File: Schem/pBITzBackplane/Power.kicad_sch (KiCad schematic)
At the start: 16 parts, among them J1 ATX-24, Q1 BSS138, SW1 SW_Push, U1 ATtiny85-20P

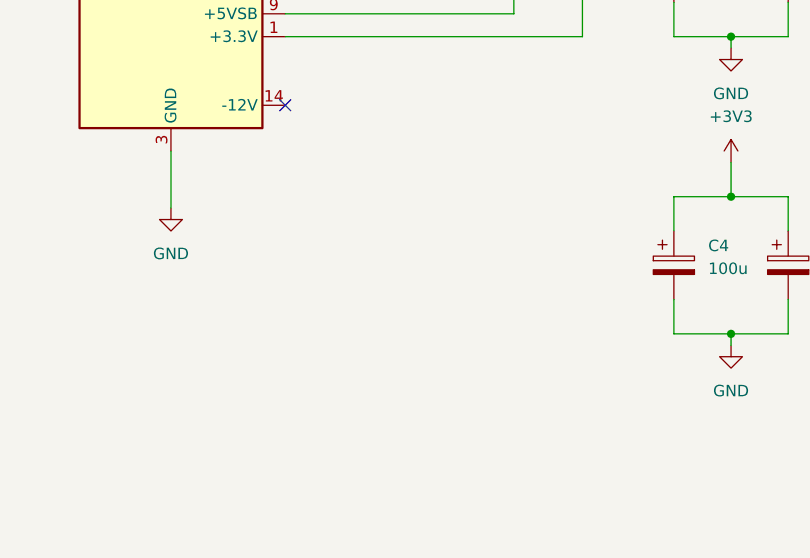
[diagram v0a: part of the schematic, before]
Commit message: Major rework:
- Updated the Mezzanine to remove the slot connector and move it to the main board (facing the back)
-    The removal of the slot allowed for the removal of the FPC connector, which was a
     major source of complexity. The mezzanine now only has the SD card and USB connectors,
     which are much cheaper and easier to work with.
- The mezzanine is now more compact and cheaper to souirce

- The main board sees the addition of the external slot connector (coming from the mezzanine)
- Added power led on the mother board for easier debugging and testing
- Removed the free floating resistors to replace them with resistor packs
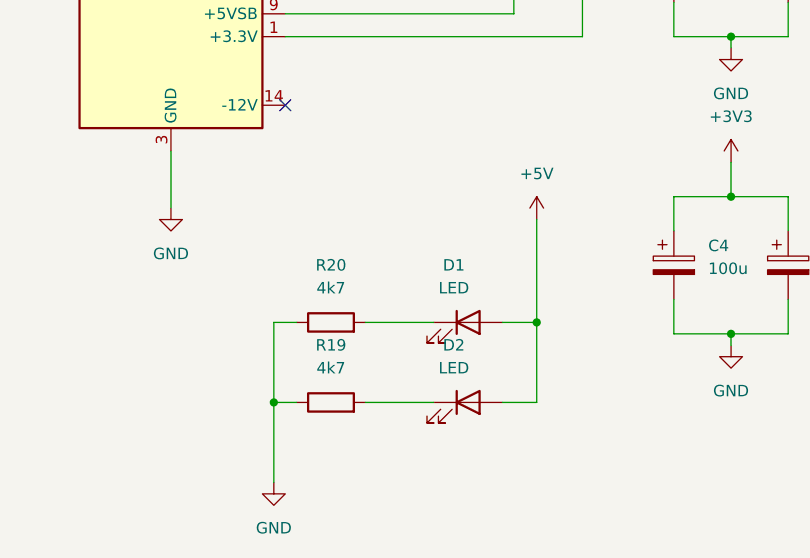
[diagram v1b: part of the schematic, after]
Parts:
- added D1: LED, LED_THT:LED_D5.0mm, symbol Device:LED
- added D2: LED, Connector_PinHeader_2.54mm:PinHeader_2x01_P2.54mm_Vertical, symbol Device:LED
- added R19, R20: 4k7, Resistor_SMD:R_0603_1608Metric, symbol Device:R
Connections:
- net +5V: now also D1.2 (A), D2.2 (A)
- net GND: now also R19.1, R20.1
- new net: D2.1 (K), R19.2
- new net: D1.1 (K), R20.2

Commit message: Cleaned up the schematic files
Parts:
- removed R2: 4k7, Resistor_SMD:R_0603_1608Metric, symbol Device:R
- added R6: 10k, Resistor_SMD:R_0603_1608Metric, symbol Device:R
- R4: value 4k7 -> 10k
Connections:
- net +5V_AON: no longer R4.2
- net GND: now also R4.1, R6.1
- net PWR_OFF_RQ: now also R4.2, U1.3 (XTAL2/PB4)
- net at Q1.1 (G), U1.5 (AREF/PB0): now also R6.2
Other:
- moved on the sheet: Q1

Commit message: Fixed board
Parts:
- removed R3: 4k7, Resistor_SMD:R_0603_1608Metric, symbol Device:R
- removed R4: 10k, Resistor_SMD:R_0603_1608Metric, symbol Device:R
- added R7, R8: 10k, Resistor_SMD:R_1206_3216Metric, symbol Device:R
- R1, R19, R20, R5, R6: footprint Resistor_SMD:R_0603_1608Metric -> Resistor_SMD:R_1206_3216Metric
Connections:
- net +5V_AON: now also R7.2, R8.2
- net ~{SHUTDOWN_RQ}: now reaches U1.2 (XTAL1/PB3)
- net ~{SHUTDOWN_RQ}: now also R7.1
- net PWR_OFF_RQ renamed ~{PWR_OFF}
- net ~{PWR_OFF}: now also R8.1

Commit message: Made the footprint bigger to facilitate soldering.
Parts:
- C1: footprint Capacitor_SMD:C_0603_1608Metric -> Capacitor_SMD:C_1206_3216Metric_Pad1.33x1.80mm_HandSolder
- R1, R19, R20, R5, R6, R7, R8: footprint Resistor_SMD:R_1206_3216Metric -> Resistor_SMD:R_1206_3216Metric_Pad1.30x1.75mm_HandSolder
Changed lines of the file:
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@@
 			)
 		)
-		(property "Footprint" "Resistor_SMD:R_1206_3216Metric"
+		(property "Footprint" "Resistor_SMD:R_1206_3216Metric_Pad1.30x1.75mm_HandSolder"
 			(at 209.55 145.288 90)
 			(hide yes)
@@
 			)
 		)
-		(property "Footprint" "Resistor_SMD:R_1206_3216Metric"
+		(property "Footprint" "Resistor_SMD:R_1206_3216Metric_Pad1.30x1.75mm_HandSolder"
 			(at 89.408 101.6 90)
 			(hide yes)
@@
 			)
 		)
-		(property "Footprint" "Resistor_SMD:R_1206_3216Metric"
+		(property "Footprint" "Resistor_SMD:R_1206_3216Metric_Pad1.30x1.75mm_HandSolder"
 			(at 118.618 138.43 90)
 			(hide yes)
@@
 			)
 		)
-		(property "Footprint" "Resistor_SMD:R_1206_3216Metric"
+		(property "Footprint" "Resistor_SMD:R_1206_3216Metric_Pad1.30x1.75mm_HandSolder"
 			(at 209.55 136.398 90)
 			(hide yes)
@@
 			)
 		)
-		(property "Footprint" "Resistor_SMD:R_1206_3216Metric"
+		(property "Footprint" "Resistor_SMD:R_1206_3216Metric_Pad1.30x1.75mm_HandSolder"
 			(at 104.14 119.888 90)
 			(hide yes)
@@
 			)
 		)
-		(property "Footprint" "Capacitor_SMD:C_0603_1608Metric"
+		(property "Footprint" "Capacitor_SMD:C_1206_3216Metric_Pad1.33x1.80mm_HandSolder"
 			(at 33.9852 95.25 0)
 			(hide yes)
@@
 			)
 		)
-		(property "Footprint" "Resistor_SMD:R_1206_3216Metric"
+		(property "Footprint" "Resistor_SMD:R_1206_3216Metric_Pad1.30x1.75mm_HandSolder"
 			(at 137.668 127 90)
 			(hide yes)
@@
 			)
 		)
-		(property "Footprint" "Resistor_SMD:R_1206_3216Metric"
+		(property "Footprint" "Resistor_SMD:R_1206_3216Metric_Pad1.30x1.75mm_HandSolder"
 			(at 103.378 138.43 90)
 			(hide yes)

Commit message: Fixed part #s
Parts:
- D1, D2, SW1: now left out of the parts list
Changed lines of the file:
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@@
 		(body_style 1)
 		(exclude_from_sim no)
-		(in_bom yes)
+		(in_bom no)
 		(on_board yes)
 		(in_pos_files yes)
@@
 		(body_style 1)
 		(exclude_from_sim no)
-		(in_bom yes)
+		(in_bom no)
 		(on_board yes)
 		(in_pos_files yes)
@@
 		(body_style 1)
 		(exclude_from_sim no)
-		(in_bom yes)
+		(in_bom no)
 		(on_board yes)
 		(in_pos_files yes)
